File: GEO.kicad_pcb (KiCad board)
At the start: 2 copper layers, 102.1 x 53.8 mm, 19 parts, among them J1 Conn_01x02, U1 Op_Amp

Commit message: changed two pin header
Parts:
- ? (x2): footprint KiCad Footprints: -> footprints:
- A1: footprint KiCad Footprints:ARDUINO_ARDUINO_MEGA_2560_REV3_A000067 -> footprints:ARDUINO_ARDUINO_MEGA_2560_REV3_A000067
- C1: footprint KiCad Footprints:CAPC1608X90 -> footprints:CAPC1608X90
- CO1: footprint KiCad Footprints:JST_B5B-XH-A -> footprints:JST_B5B-XH-A
- Clk1: footprint KiCad Footprints:TE_5-146280-5 -> footprints:TE_5-146280-5
- H1, H2: footprint MountingHole:MountingHole_2.1mm -> footprints:MountingHole_2.1mm
- J1: footprint Connector_PinHeader_2.00mm:PinHeader_1x02_P2.00mm_Vertical -> footprints:PinSocket_1x02_P2.54mm_Vertical
- LCD1: footprint Connector_FFC-FPC:TE_84952-9_1x09-1MP_P1.0mm_Horizontal -> footprints:TE_84952-9_1x09-1MP_P1.0mm_Horizontal
- PM1: footprint KiCad Footprints:JST_SM08B-GHS-TB(LF)(SN) -> footprints:JST_SM08B-GHS-TB(LF)(SN)
- R1, R2: footprint Resistor_THT:R_Axial_DIN0309_L9.0mm_D3.2mm_P12.70mm_Horizontal -> footprints:R_Axial_DIN0309_L9.0mm_D3.2mm_P12.70mm_Horizontal
- R3, R4: footprint KiCad Footprints:R0402 -> footprints:R0402
- SD1: footprint KiCad Footprints:JST_B6B-XH-A(LF)(SN) -> footprints:JST_B6B-XH-A(LF)(SN)
- TEMP1: footprint KiCad Footprints:JST_B4B-XH-A(LF)(SN) -> footprints:JST_B4B-XH-A(LF)(SN)
- U1: footprint Package_TO_SOT_SMD:SOT-353_SC-70-5 -> footprints:SOT-353_SC-70-5
- U2: footprint KiCad Footprints:DFR1015 Buck_Converter -> footprints:DFR1015 Buck_Converter
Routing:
- net /5V: track 181.5 -> 178.0 mm
- net /OP_AMP_OUT: track 9.11 -> 8.61 mm

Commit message: flip buck converter and add screw terminal, gen gerber files
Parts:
- removed ? (x2): , footprints:
- removed H1, H2: MountingHole, footprints:MountingHole_2.1mm
- added J2: Screw_Terminal_01x02, TerminalBlock:TerminalBlock_MaiXu_MX126-5.0-02P_1x02_P5.00mm, F.Cu at (108.5, 114.9)
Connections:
- U2 pad 1: /BAT_IN -> /5V
- U2 pad 3: /5V -> /BAT_IN
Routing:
- net /3.3V: track 86.4 -> 97.5 mm
- net /BAT_IN: track 85.2 -> 83.0 mm, vias 1 -> 2
- net /5V: track 178.0 -> 179.3 mm

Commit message: removed Vref circuitry from CO sensor and wired Vref to pin A2
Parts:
- removed C1: .1u, footprints:CAPC1608X90
- removed J1: Conn_01x02, footprints:PinSocket_1x02_P2.54mm_Vertical
- removed R3, R4: 10k, footprints:R0402
- removed U1: Op_Amp, footprints:SOT-353_SC-70-5
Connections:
- A1 pad AD2: unconnected-(A1-PadAD2) -> /CO_VREF
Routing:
- net /CO_VREF: track 14.6 -> 56.5 mm
- net /5V: track 179.3 -> 150.2 mm, vias 2 -> 1
- net /GND: track 26.2 -> 0.00 mm, vias 5 -> 6
- net /3.3V: track 97.5 -> 87.3 mm
- net /OP_AMP_OUT: track 8.61 -> 0.00 mm
- net /1.65V: track 5.88 -> 0.00 mm
- net /CO_VGAS: track 54.0 -> 54.5 mm

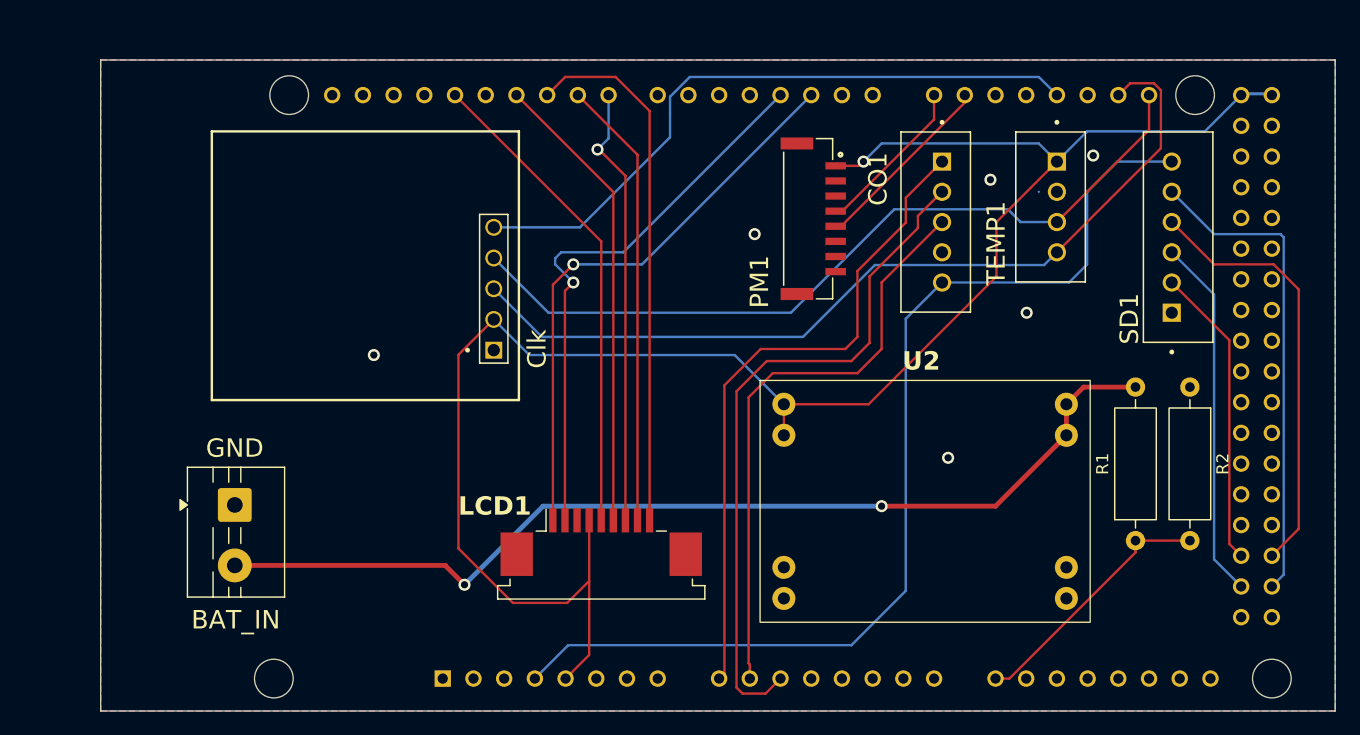
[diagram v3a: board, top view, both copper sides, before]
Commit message: gerber 03-24-26, add VRef pin
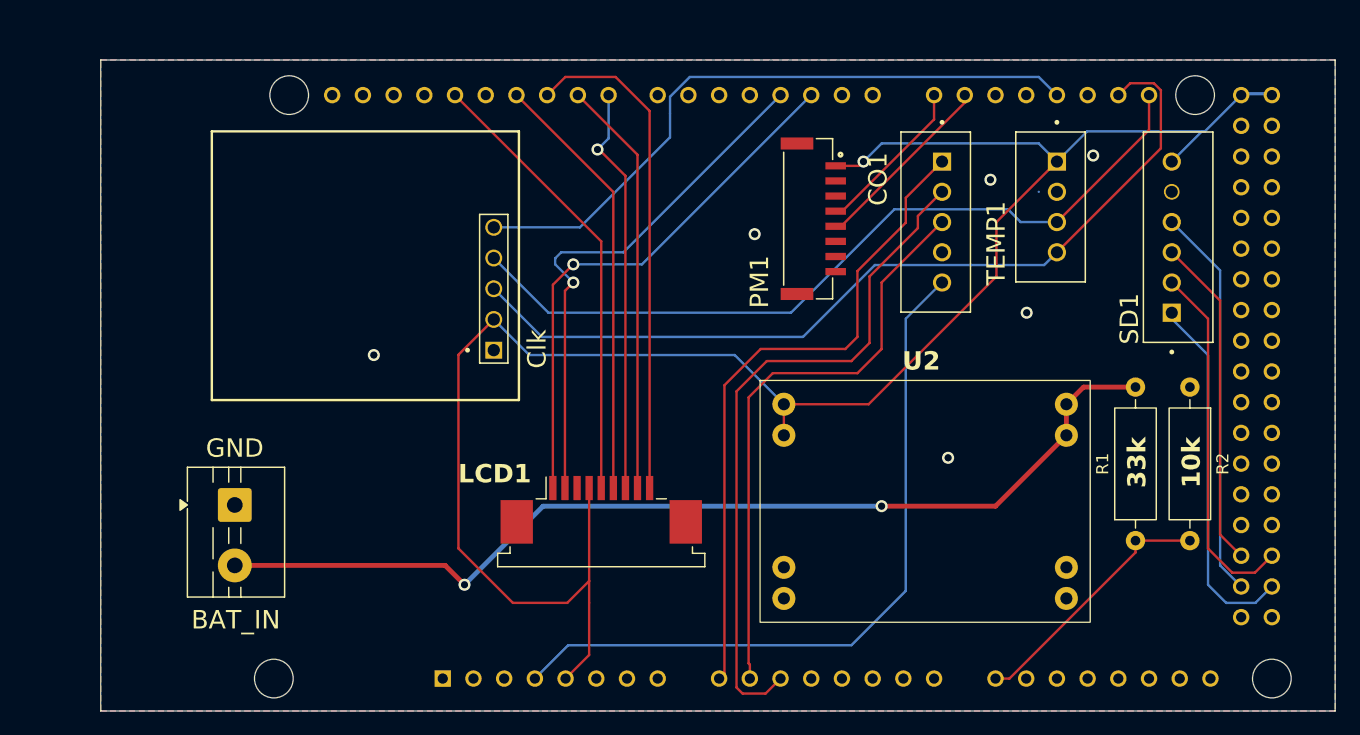
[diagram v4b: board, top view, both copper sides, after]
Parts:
- R1: value R -> 33k
- R2: value R -> 10k
- moved LCD1 2.67 mm to (138.8, 115.3)
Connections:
- SD1 pad 1: /GND -> /SD_CS
- SD1 pad 2: /SD_MISO -> /SD_MOSI
- SD1 pad 3: /SD_CLK -> /SD_MISO
- SD1 pad 4: /SD_MOSI -> /SD_CLK
- SD1 pad 5: /SD_CS -> /GND
- SD1 pad 6: /3.3V -> /5V
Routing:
- net /3.3V: track 87.3 -> 60.4 mm
- net /SD_CS: track 40.1 -> 30.2 mm
- net /5V: track 150.2 -> 156.9 mm
- net /SD_MOSI: track 35.8 -> 29.9 mm
- net /LCD_SDA: track 38.5 -> 35.8 mm
- net /LCD_SCK: track 40.2 -> 37.5 mm
- net /LCD_RES: track 36.6 -> 33.9 mm
- net /LCD_DC: track 37.2 -> 34.5 mm
- net /LCD_CS: track 44.1 -> 41.4 mm
- net /BTN2: track 47.4 -> 44.7 mm
- net /BTN1: track 46.8 -> 44.1 mm
- net /SD_MISO: track 25.0 -> 27.5 mm
- net /SD_CLK: track 30.0 -> 32.5 mm
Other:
- board text added: "10k"
- board text added: "33k"
